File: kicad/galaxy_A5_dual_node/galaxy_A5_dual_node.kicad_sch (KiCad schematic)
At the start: 88 parts, among them J1 Conn, J2 Conn, J3 USB_C_Receptacle_PowerOnly_6P, J4 Conn_01x02_Socket, J5 Conn_01x02_Socket, Q1 DTC143Z, Q2 DTC143Z, Q3 DTC143Z, Q4 DTC143Z, SW1 SW_MAIN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

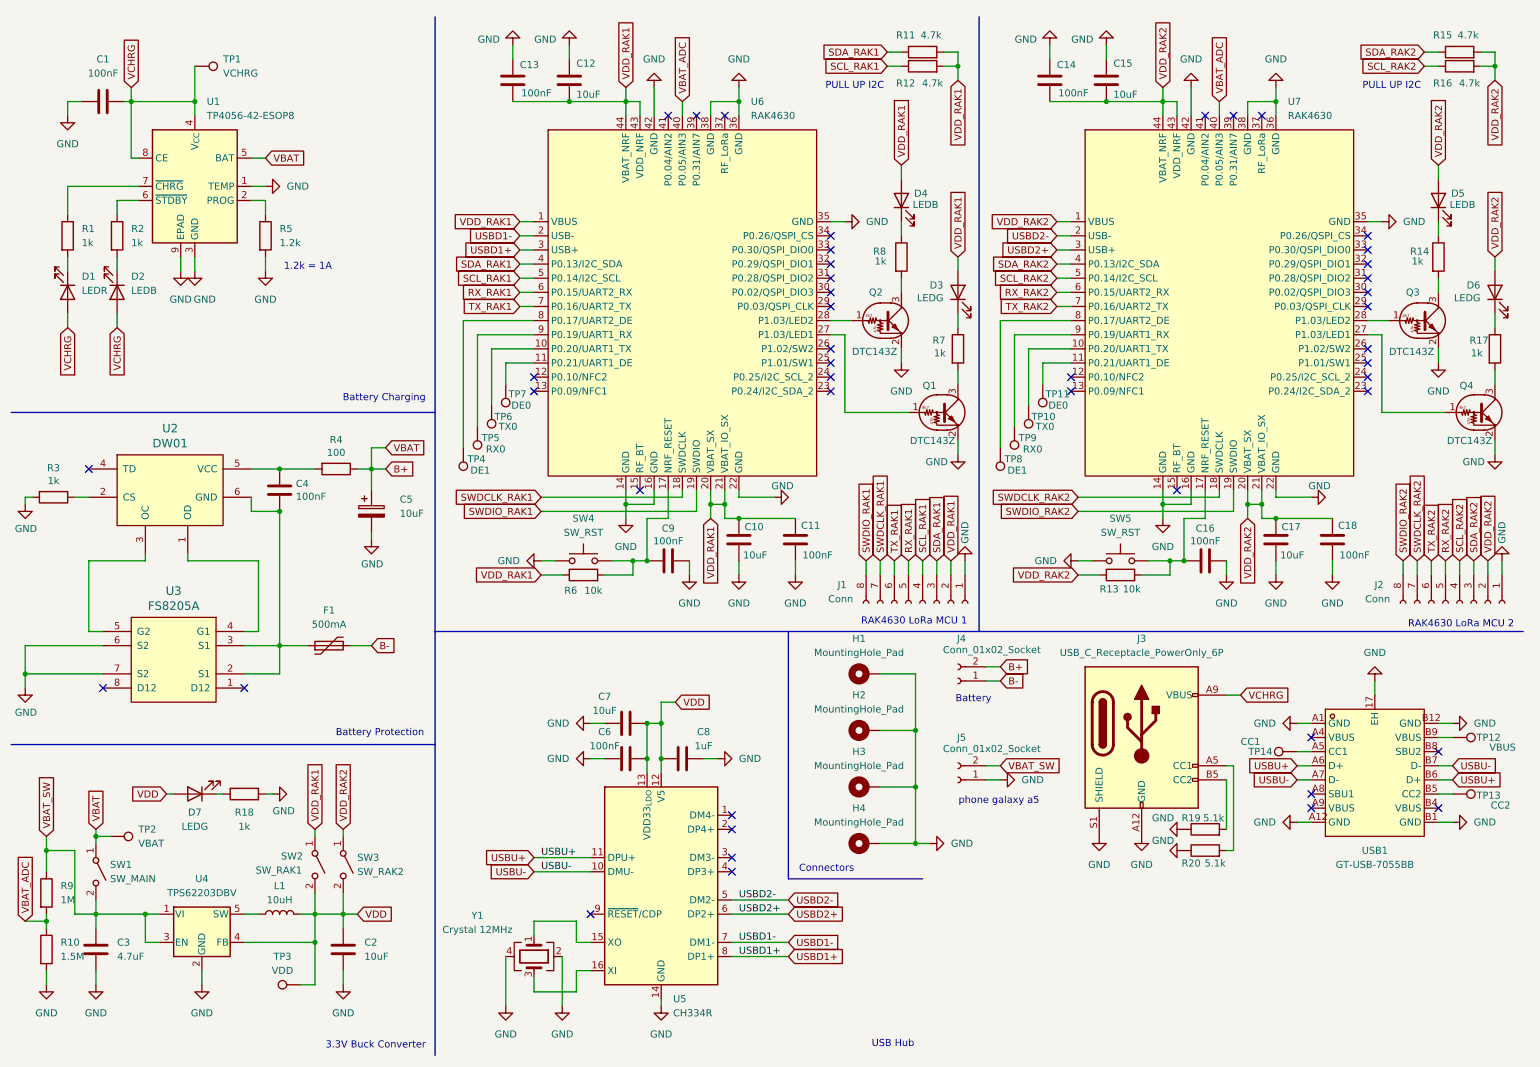
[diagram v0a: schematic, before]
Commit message: fixed USB CC, VBUS RAK
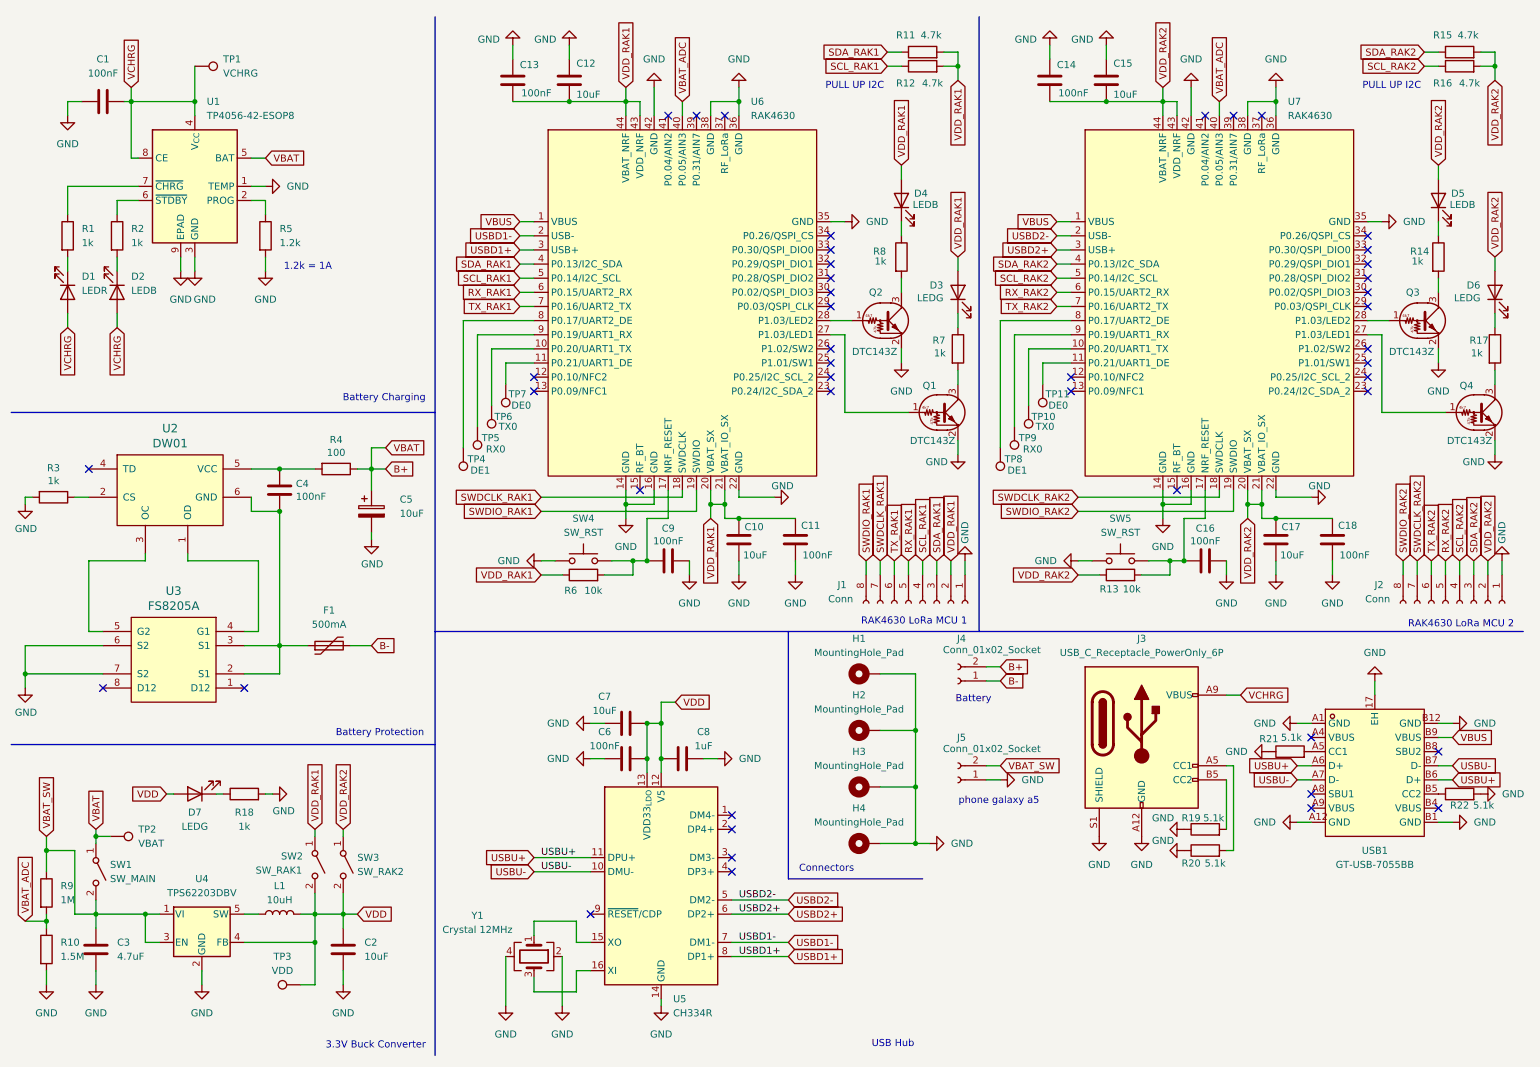
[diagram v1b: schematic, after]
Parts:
- removed TP12: VBUS, TestPoint:TestPoint_Pad_D1.5mm, symbol Connector:TestPoint
- removed TP13: CC2, TestPoint:TestPoint_Pad_D1.5mm, symbol Connector:TestPoint
- removed TP14: CC1, TestPoint:TestPoint_Pad_D1.5mm, symbol Connector:TestPoint
- added R21, R22: 5.1k, Resistor_SMD:R_0805_2012Metric, symbol Device:R
- R19, R20: footprint (none) -> Resistor_SMD:R_0805_2012Metric
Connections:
- net GND: now also R21.1, R22.2
- net VDD_RAK1: no longer U6.1 (VBUS)
- net VDD_RAK2: no longer U7.1 (VBUS)
- net at USB1.A5 (CC1): now also R21.2
- net VBUS: now reaches USB1.B9 (VBUS)
- net VBUS: now also U6.1 (VBUS), U7.1 (VBUS)
- net at USB1.B5 (CC2): now also R22.1
